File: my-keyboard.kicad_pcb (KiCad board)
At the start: 2 copper layers, 304.8 x 115.9 mm, 171 parts, among them SW1 SW_Push, U1 ATmega32U4-AU, Y1 16MHz

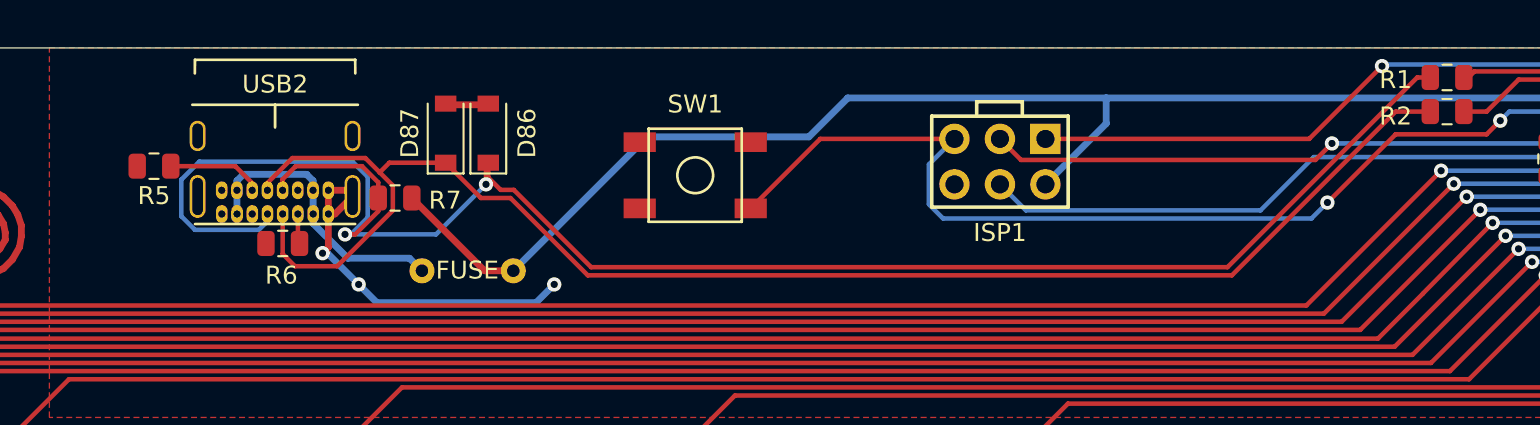
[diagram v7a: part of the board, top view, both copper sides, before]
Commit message: different usb footprint
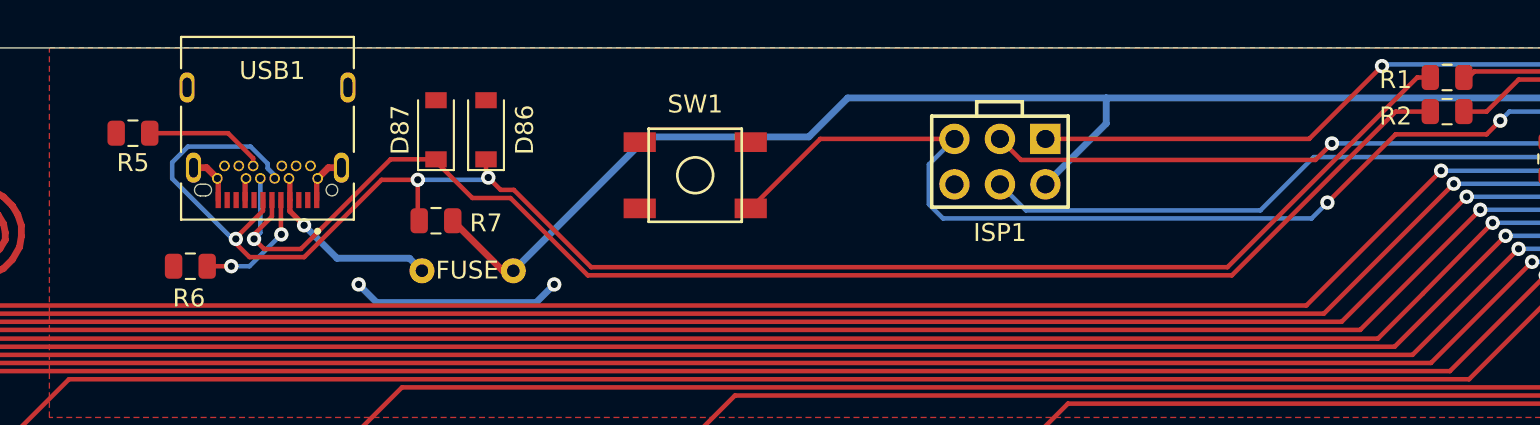
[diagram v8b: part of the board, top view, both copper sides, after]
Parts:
- MX0: renamed from MX0-0; value Esc -> 1
- MX10: renamed from MX10-0; value 0 -> 1
- MX11: renamed from MX11-0; value - -> 1
- MX12: renamed from MX12-0; value = -> 1
- MX13: renamed from MX13-0; value Backspace -> 1
- MX14: renamed from MX15-0; value Tilde -> 1
- MX15: renamed from MX0-1; value Tab -> 1
- MX16: renamed from MX1-1; value Q -> 1
- MX17: renamed from MX2-1; value W -> 1
- MX18: renamed from MX3-1; value E -> 1
- MX19: renamed from MX4-1; value R -> 1
- MX2: renamed from MX2-0; value 2 -> 1
- MX20: renamed from MX5-1; value T -> 1
- MX21: renamed from MX6-1; value Y -> 1
- MX22: renamed from MX7-1; value U -> 1
- MX23: renamed from MX8-1; value I -> 1
- MX24: renamed from MX9-1; value O -> 1
- MX25: renamed from MX10-1; value P -> 1
- MX26: renamed from MX11-1; value [ -> 1
- MX27: renamed from MX12-1; value ] -> 1
- MX28: renamed from MX13-1; value \ -> 1
- MX29: renamed from MX15-1; value Del -> 1
- MX3: renamed from MX3-0; value 3 -> 1
- MX30: renamed from MX0-2; value Caps Lock -> 1
- MX31: renamed from MX1-2; value A -> 1
- MX32: renamed from MX2-2; value S -> 1
- MX33: renamed from MX3-2; value D -> 1
- MX34: renamed from MX4-2; value F -> 1
- MX35: renamed from MX5-2; value G -> 1
- MX36: renamed from MX6-2; value H -> 1
- MX37: renamed from MX7-2; value J -> 1
- MX38: renamed from MX8-2; value K -> 1
- MX39: renamed from MX9-2; value L -> 1
- MX4: renamed from MX4-0; value 4 -> 1
- MX40: renamed from MX10-2; value ; -> 1
- MX41: renamed from MX11-2; value ' -> 1
- MX42: renamed from MX12-2; value return -> 1
- MX43: renamed from MX15-2; value PgUp -> 1
- MX44: renamed from MX0-3; value Shift -> 1
- MX45: renamed from MX2-3; value Z -> 1
- MX46: renamed from MX3-3; value X -> 1
- MX47: renamed from MX4-3; value C -> 1
- MX48: renamed from MX5-3; value V -> 1
- MX49: renamed from MX6-3; value B -> 1
- MX5: renamed from MX5-0; value 5 -> 1
- MX50: renamed from MX7-3; value N -> 1
- MX51: renamed from MX8-3; value M -> 1
- MX52: renamed from MX9-3; value , -> 1
- MX53: renamed from MX10-3; value . -> 1
- MX54: renamed from MX11-3; value / -> 1
- MX55: renamed from MX12-3; value Shift -> 1
- MX56: renamed from MX14-3; value Up -> 1
- MX57: renamed from MX15-3; value PgDn -> 1
- MX58: renamed from MX0-4; value LCtrl -> 1
- MX59: renamed from MX1-4; value LMeta -> 1
- MX6: renamed from MX6-0; value 6 -> 1
- MX60: renamed from MX2-4; value Alt -> 1
- MX61: renamed from MX6-4; value Space -> 1
- MX62: renamed from MX10-4; value Fn -> 1
- MX63: renamed from MX11-4; value Alt -> 1
- MX64: renamed from MX13-4; value Left -> 1
- MX65: renamed from MX14-4; value Down -> 1
- MX66: renamed from MX15-4; value Right -> 1
- MX7: renamed from MX7-0; value 7 -> 1
- MX8: renamed from MX8-0; value 8 -> 1
- MX9: renamed from MX9-0; value 9 -> 1
- USB1: renamed from USB2; footprint cftkb:USB_C_GCT_USB4085 -> SnapEDA:AMPHENOL_10137061-00021LF
- moved USB1 5.72 mm to (280.2, 109.5)
- moved R6 5.31 mm to (272.3, 113.8)
- moved R7 2.62 mm to (286.0, 111.3)
- moved R5 2.18 mm to (269.1, 106.4)
- moved D87 0.57 mm to (286.0, 106.2)
- moved D86 0.23 mm to (288.8, 106.2)
- renumbered MX1-0 to MX1
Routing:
- net /D-: track 103.2 -> 94.6 mm, vias 2 -> 3
- net GND: track 91.6 -> 84.9 mm, vias 6 -> 5
- net Net-(R6-Pad2): track 1.64 -> 6.81 mm, vias 0 -> 2
- net /D+: track 85.3 -> 80.5 mm, vias 0 -> 1
- net VCC: track 16.2 -> 11.7 mm, vias 0 -> 1
- net +5V: track 146.1 -> 143.3 mm
- net Net-(R5-Pad1): track 5.34 -> 6.78 mm
